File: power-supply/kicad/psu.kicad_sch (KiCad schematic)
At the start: 17 parts, among them J3 SSQ-103-03-G-D, U1 LM2776, U3 TPS72301DBVR, U5 TPS79333DBVR

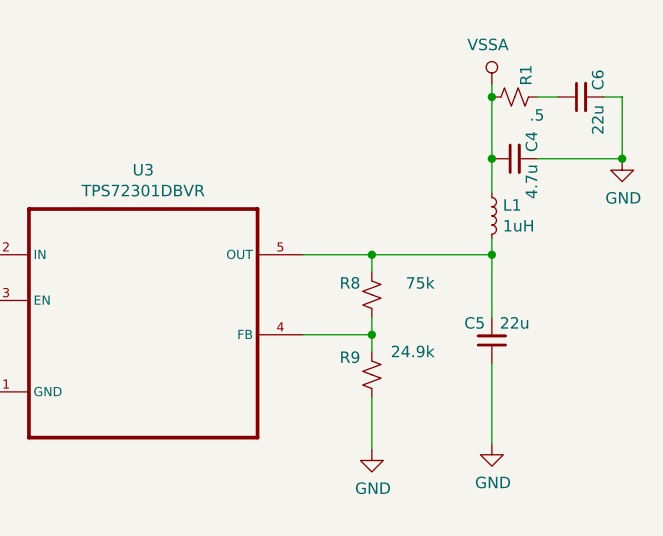
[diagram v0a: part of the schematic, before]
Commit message: Lower negative voltage rail slightly
Depending on the USB +5 load, the length of the cable, etc the voltage could dip enough that the regulator would drop out under very heavy load.  Decreasing to 4.3v prevents this but still enables >1.3v output.
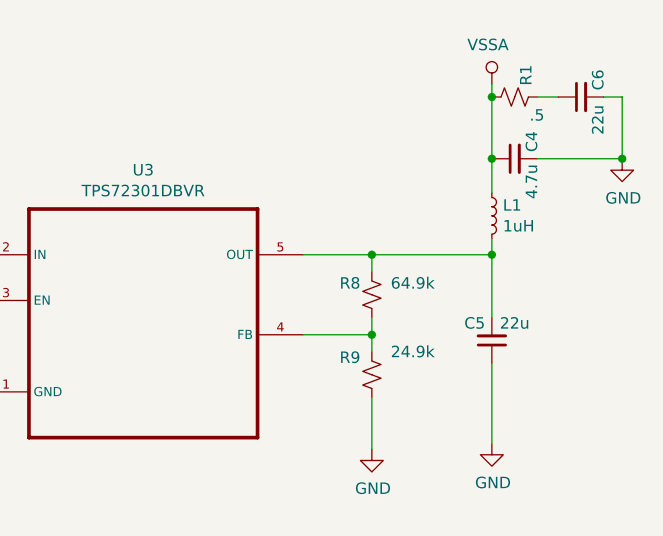
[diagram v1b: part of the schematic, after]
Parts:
- R8: value 75k -> 64.9k
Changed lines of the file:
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@@
       (effects (font (size 1.27 1.27)) (justify left))
     )
-    (property "Value" "75k" (id 1) (at 257.81 114.935 0)
+    (property "Value" "64.9k" (id 1) (at 257.81 114.935 0)
       (effects (font (size 1.27 1.27)) (justify left))
     )

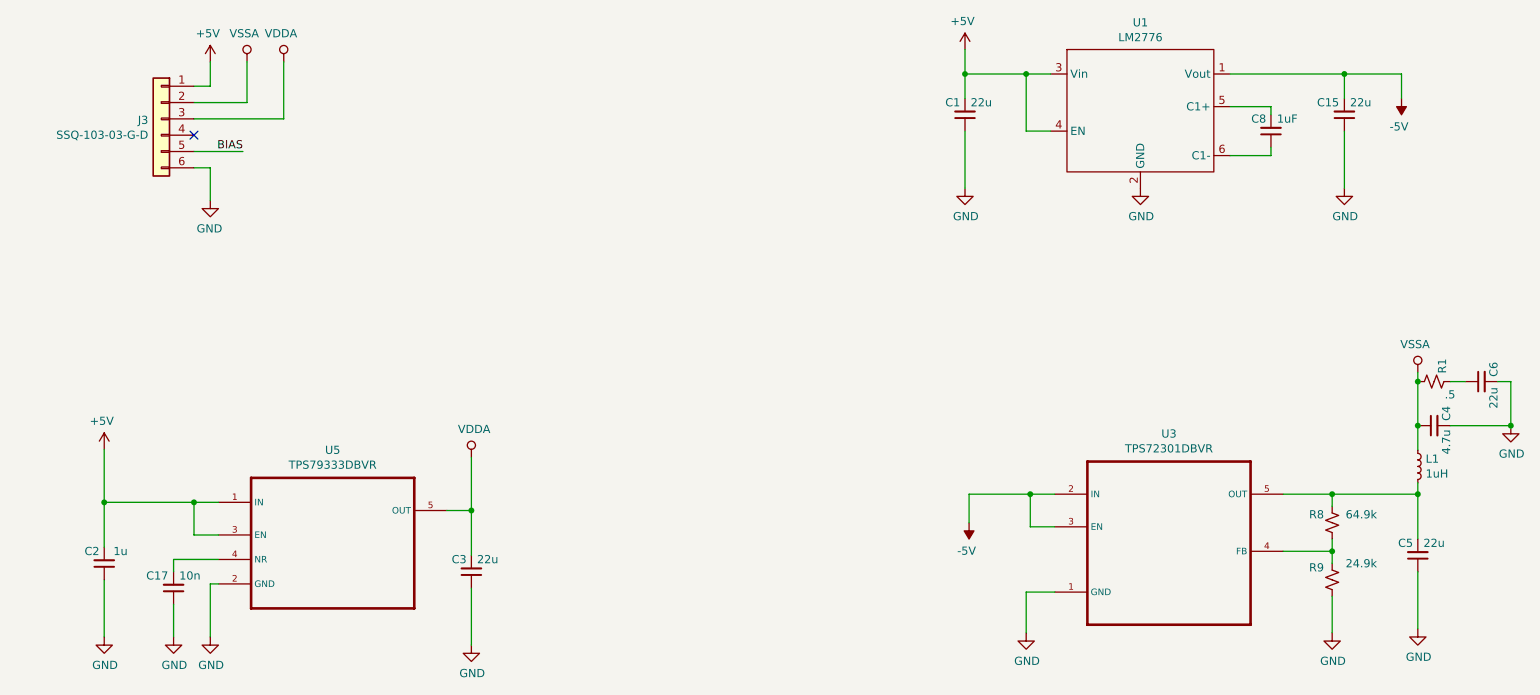
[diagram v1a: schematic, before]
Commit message: Remove unneeded LC filter from power supply negative rail
In testing it made no difference and complicated the layout.
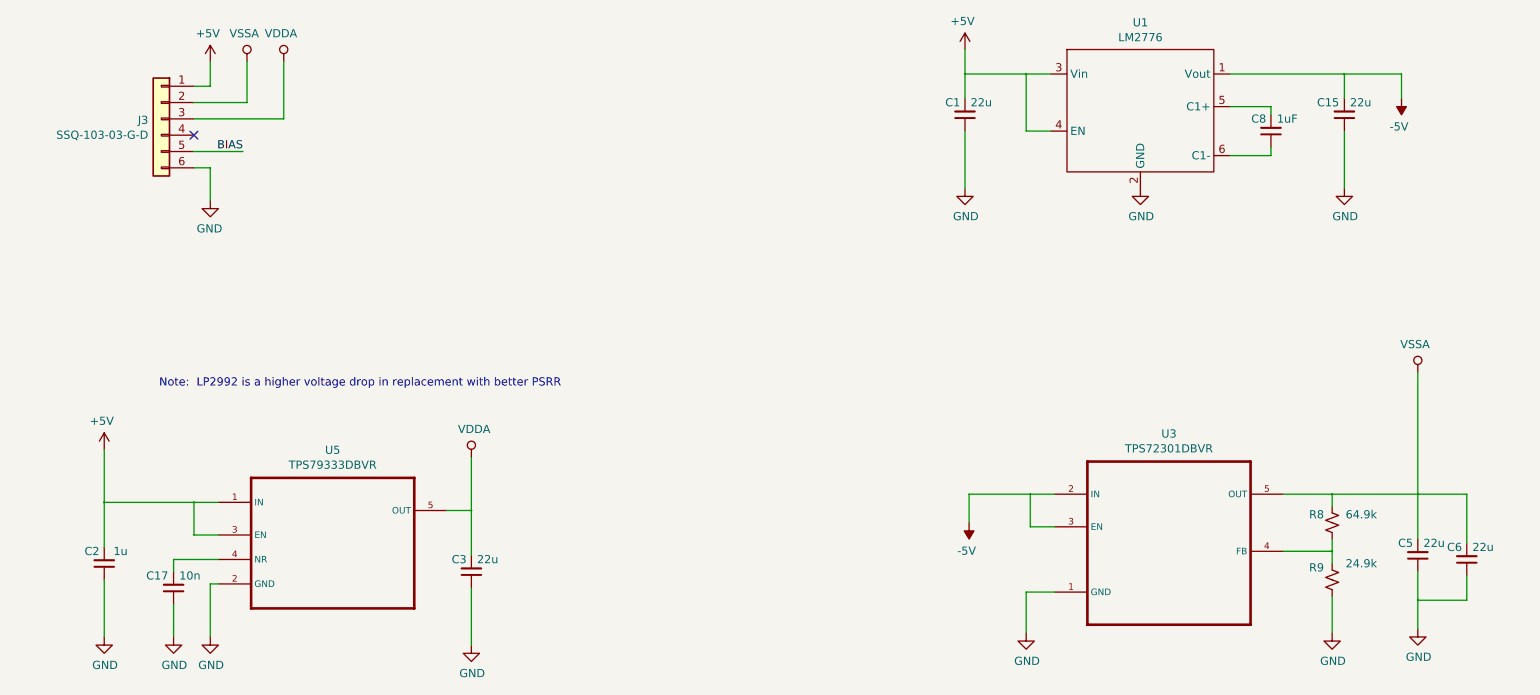
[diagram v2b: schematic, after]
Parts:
- removed C4: 4.7u, footprints:C_0603_1608Metric, symbol Device:C_Small
- removed L1: 1uH, footprints:L_0603_1608Metric, symbol Device:L_Small
- removed R1: .5, footprints:R_0603_1608Metric, symbol Device:R_Small_US
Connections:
- net GND: now also C6.1; no longer C6.2
- net VSSA: now also C5.2, C6.2, R8.2, U3.5 (OUT)
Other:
- note added: "Note: LP2992 is a higher voltage drop in replacement with better PSRR"
- moved on the sheet: C6
